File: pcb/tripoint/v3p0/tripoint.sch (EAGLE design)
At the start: 40 parts, among them T1 HHM1595A1, U1 STM32F091CC, U2 DW1000, U3 SKY13317, U4 LXDC2HN18A, X1 FA-128

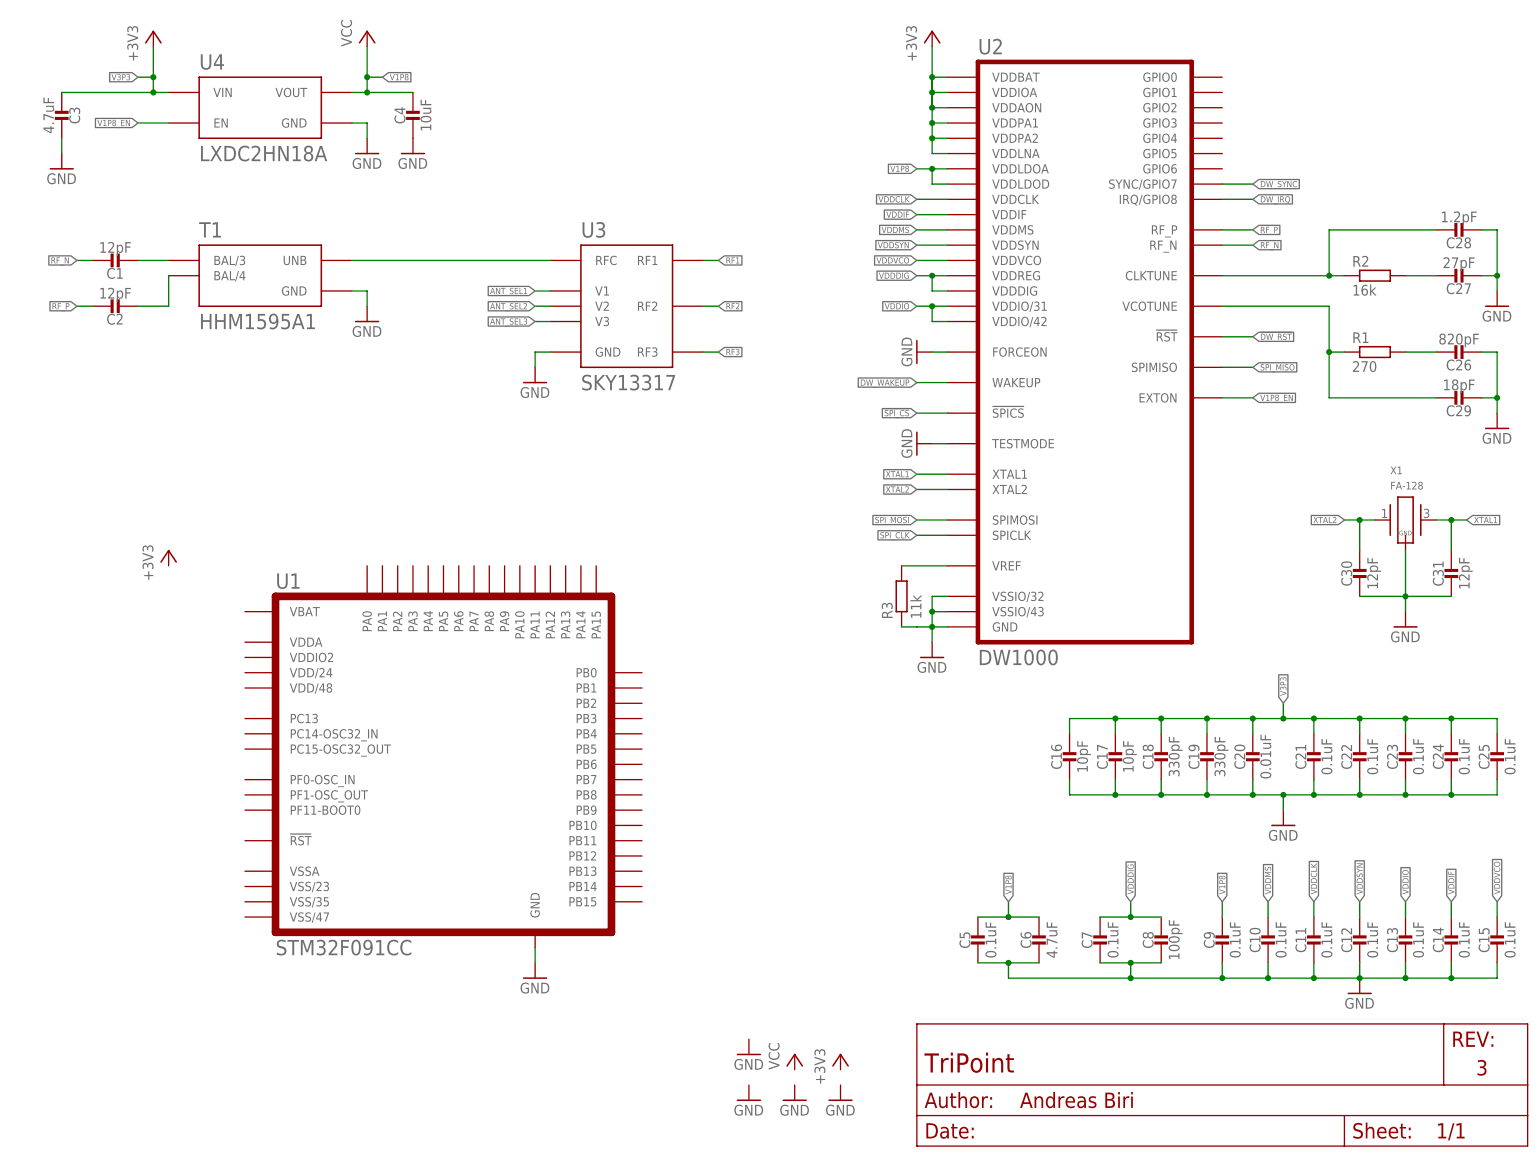
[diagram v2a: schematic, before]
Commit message: added oscillators
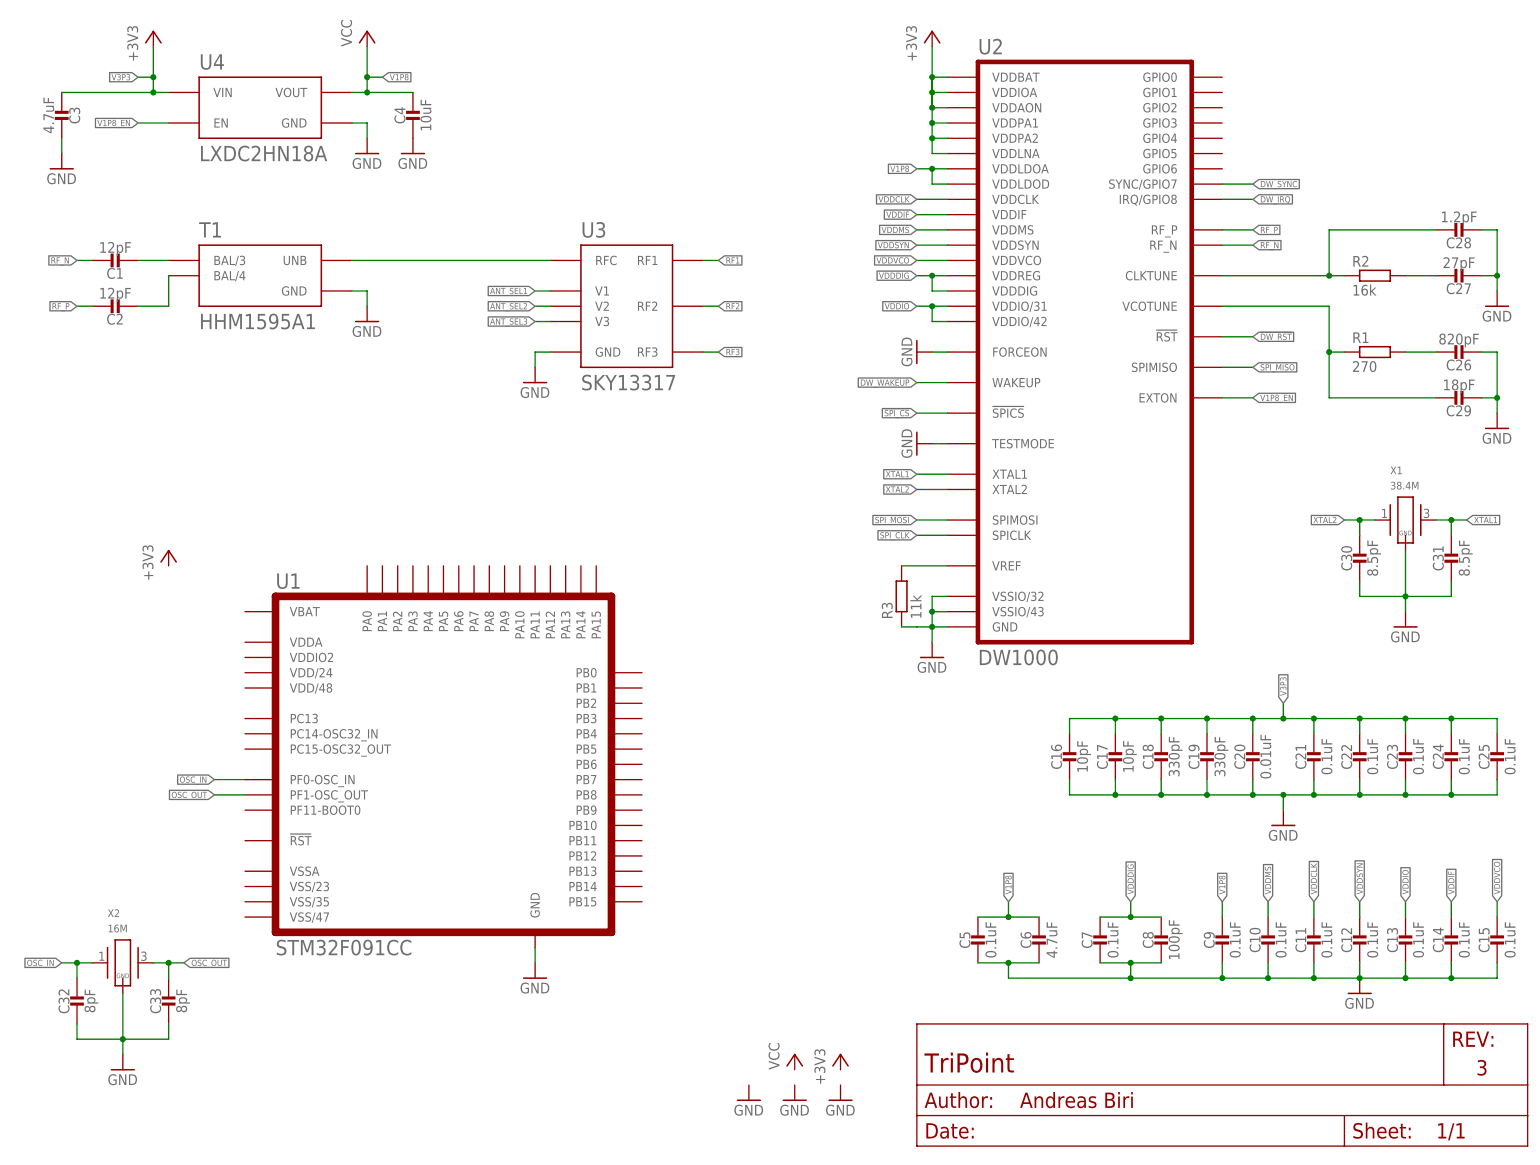
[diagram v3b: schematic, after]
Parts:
- added C32, C33: 8pF, passives:CAPACITOR0201_CAP
- added X2: 16M, crystals:FA-20H
- C30, C31: value 12pF -> 8.5pF
- X1: value FA-128 -> 38.4M; device crystals:FA-128 -> crystals:FA-20H; DESCRIPTION (none) -> 38.4MHz ±10ppm Crystal 8.5pF 40 Ohms 4-SMD, No Lead; DIGIKEY (none) -> SER3631CT-ND
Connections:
- new net OSC_IN: C32.1, U1.PF0-OSC_IN, X2.1
- new net OSC_OUT: C33.1, U1.PF1-OSC_OUT, X2.2
- net GND: now also C32.2, C33.2, X2.GND
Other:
- moved on the sheet: C30, C31
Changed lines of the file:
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@@
 <part name="SUPPLY17" library="umich" deviceset="GND" device=""/>
 <part name="SUPPLY18" library="umich" deviceset="GND" device=""/>
-<part name="X1" library="crystals" deviceset="FA-128" device=""/>
-<part name="C30" library="passives" deviceset="CAPACITOR" device="0201_CAP" value="12pF"/>
-<part name="C31" library="passives" deviceset="CAPACITOR" device="0201_CAP" value="12pF"/>
+<part name="C30" library="passives" deviceset="CAPACITOR" device="0201_CAP" value="8.5pF"/>
+<part name="C31" library="passives" deviceset="CAPACITOR" device="0201_CAP" value="8.5pF"/>
 <part name="+3V1" library="supply1" library_urn="urn:adsk.eagle:library:371" deviceset="+3V3" device=""/>
 <part name="+3V3" library="supply1" library_urn="urn:adsk.eagle:library:371" deviceset="+3V3" device=""/>
+<part name="C32" library="passives" deviceset="CAPACITOR" device="0201_CAP" value="8pF"/>
+<part name="C33" library="passives" deviceset="CAPACITOR" device="0201_CAP" value="8pF"/>
+<part name="X1" library="crystals" deviceset="FA-20H" device="" value="38.4M">
+<attribute name="DESCRIPTION" value="38.4MHz ±10ppm Crystal 8.5pF 40 Ohms 4-SMD, No Lead"/>
+<attribute name="DIGIKEY" value="SER3631CT-ND"/>
+</part>
+<part name="X2" library="crystals" deviceset="FA-20H" device="" value="16M">
+<attribute name="DESCRIPTION" value="16MHz ±10ppm Crystal 8pF 80 Ohms 4-SMD, No Lead"/>
+<attribute name="DIGIKEY" value="SER3913CT-ND"/>
+</part>
 </parts>
 <sheets>
@@
 <instance part="C29" gate="G$1" x="241.3" y="124.46" rot="R90"/>
 <instance part="SUPPLY12" gate="1" x="152.4" y="132.08" rot="R270"/>
-<instance part="SUPPLY13" gate="1" x="124.46" y="15.24"/>
+<instance part="SUPPLY13" gate="1" x="20.32" y="12.7"/>
 <instance part="SUPPLY14" gate="1" x="124.46" y="7.62"/>
 <instance part="SUPPLY15" gate="1" x="152.4" y="116.84" rot="R270"/>
@@
 <instance part="SUPPLY17" gate="1" x="154.94" y="81.28"/>
 <instance part="SUPPLY18" gate="1" x="233.68" y="86.36"/>
-<instance part="X1" gate="G$1" x="233.68" y="104.14"/>
-<instance part="C30" gate="G$1" x="226.06" y="96.52"/>
-<instance part="C31" gate="G$1" x="241.3" y="96.52"/>
+<instance part="C30" gate="G$1" x="226.06" y="99.06"/>
+<instance part="C31" gate="G$1" x="241.3" y="99.06"/>
 <instance part="+3V1" gate="G$1" x="27.94" y="99.06"/>
 <instance part="+3V3" gate="G$1" x="139.7" y="15.24"/>
+<instance part="C32" gate="G$1" x="12.7" y="25.4"/>
+<instance part="C33" gate="G$1" x="27.94" y="25.4"/>
+<instance part="X1" gate="X1" x="233.68" y="104.14">
+<attribute name="DIGIKEY" x="233.68" y="104.14" size="1.778" layer="96" display="off"/>
+<attribute name="DESCRIPTION" x="233.68" y="104.14" size="1.778" layer="96" display="off"/>
+</instance>
+<instance part="X2" gate="X1" x="20.32" y="30.48">
+<attribute name="DIGIKEY" x="20.32" y="30.48" size="1.778" layer="96" display="off"/>
+<attribute name="DESCRIPTION" x="20.32" y="30.48" size="1.778" layer="96" display="off"/>
+</instance>
 </instances>
 <busses>
@@
 </segment>
 <segment>
+<pinref part="U2" gate="U1" pin="TESTMODE"/>
+<wire x1="157.48" y1="116.84" x2="154.94" y2="116.84" width="0.1524" layer="91"/>
+<pinref part="SUPPLY15" gate="1" pin="GND"/>
+</segment>
+<segment>
+<pinref part="U2" gate="U1" pin="FORCEON"/>
+<wire x1="157.48" y1="132.08" x2="154.94" y2="132.08" width="0.1524" layer="91"/>
+<pinref part="SUPPLY12" gate="1" pin="GND"/>
+</segment>
+<segment>
 <pinref part="C30" gate="G$1" pin="2"/>
+<wire x1="226.06" y1="93.98" x2="226.06" y2="91.44" width="0.1524" layer="91"/>
 <pinref part="C31" gate="G$1" pin="2"/>
 <wire x1="226.06" y1="91.44" x2="233.68" y2="91.44" width="0.1524" layer="91"/>
 <wire x1="233.68" y1="91.44" x2="241.3" y2="91.44" width="0.1524" layer="91"/>
+<wire x1="241.3" y1="91.44" x2="241.3" y2="93.98" width="0.1524" layer="91"/>
+<pinref part="X1" gate="X1" pin="GND"/>
+<wire x1="233.68" y1="99.06" x2="233.68" y2="91.44" width="0.1524" layer="91"/>
+<junction x="233.68" y="91.44"/>
+<pinref part="SUPPLY18" gate="1" pin="GND"/>
 <wire x1="233.68" y1="91.44" x2="233.68" y2="88.9" width="0.1524" layer="91"/>
-<junction x="233.68" y="91.44"/>
-<pinref part="X1" gate="G$1" pin="GND"/>
-<wire x1="233.68" y1="99.06" x2="233.68" y2="91.44" width="0.1524" layer="91"/>
-<pinref part="SUPPLY18" gate="1" pin="GND"/>
-</segment>
-<segment>
-<pinref part="U2" gate="U1" pin="TESTMODE"/>
-<wire x1="157.48" y1="116.84" x2="154.94" y2="116.84" width="0.1524" layer="91"/>
-<pinref part="SUPPLY15" gate="1" pin="GND"/>
-</segment>
-<segment>
-<pinref part="U2" gate="U1" pin="FORCEON"/>
-<wire x1="157.48" y1="132.08" x2="154.94" y2="132.08" width="0.1524" layer="91"/>
-<pinref part="SUPPLY12" gate="1" pin="GND"/>
+</segment>
+<segment>
+<pinref part="C32" gate="G$1" pin="2"/>
+<wire x1="12.7" y1="20.32" x2="12.7" y2="17.78" width="0.1524" layer="91"/>
+<pinref part="C33" gate="G$1" pin="2"/>
+<wire x1="12.7" y1="17.78" x2="20.32" y2="17.78" width="0.1524" layer="91"/>
+<wire x1="20.32" y1="17.78" x2="27.94" y2="17.78" width="0.1524" layer="91"/>
+<wire x1="27.94" y1="17.78" x2="27.94" y2="20.32" width="0.1524" layer="91"/>
+<pinref part="X2" gate="X1" pin="GND"/>
+<wire x1="20.32" y1="25.4" x2="20.32" y2="17.78" width="0.1524" layer="91"/>
+<junction x="20.32" y="17.78"/>
+<pinref part="SUPPLY13" gate="1" pin="GND"/>
+<wire x1="20.32" y1="17.78" x2="20.32" y2="15.24" width="0.1524" layer="91"/>
 </segment>
 </net>
@@
 <net name="XTAL2" class="0">
 <segment>
-<pinref part="X1" gate="G$1" pin="1"/>
 <wire x1="228.6" y1="104.14" x2="226.06" y2="104.14" width="0.1524" layer="91"/>
 <pinref part="C30" gate="G$1" pin="1"/>
 <wire x1="226.06" y1="104.14" x2="223.52" y2="104.14" width="0.1524" layer="91"/>
-<wire x1="226.06" y1="104.14" x2="226.06" y2="99.06" width="0.1524" layer="91"/>
+<wire x1="226.06" y1="104.14" x2="226.06" y2="101.6" width="0.1524" layer="91"/>
 <junction x="226.06" y="104.14"/>
 <label x="223.52" y="104.14" size="1.016" layer="95" rot="R180" xref="yes"/>
+<pinref part="X1" gate="X1" pin="1"/>
 </segment>
 <segment>
@@
 <net name="XTAL1" class="0">
 <segment>
-<pinref part="X1" gate="G$1" pin="2"/>
-<wire x1="238.76" y1="104.14" x2="241.3" y2="104.14" width="0.1524" layer="91"/>
 <pinref part="C31" gate="G$1" pin="1"/>
 <wire x1="241.3" y1="104.14" x2="243.84" y2="104.14" width="0.1524" layer="91"/>
-<wire x1="241.3" y1="104.14" x2="241.3" y2="99.06" width="0.1524" layer="91"/>
+<wire x1="241.3" y1="104.14" x2="241.3" y2="101.6" width="0.1524" layer="91"/>
 <junction x="241.3" y="104.14"/>
 <label x="243.84" y="104.14" size="1.016" layer="95" xref="yes"/>
+<wire x1="241.3" y1="104.14" x2="238.76" y2="104.14" width="0.1524" layer="91"/>
+<pinref part="X1" gate="X1" pin="2"/>
 </segment>
 <segment>
@@
 </segment>
 </net>
+<net name="OSC_IN" class="0">
+<segment>
+<pinref part="C32" gate="G$1" pin="1"/>
+<wire x1="15.24" y1="30.48" x2="12.7" y2="30.48" width="0.1524" layer="91"/>
+<wire x1="12.7" y1="30.48" x2="12.7" y2="27.94" width="0.1524" layer="91"/>
+<wire x1="12.7" y1="30.48" x2="10.16" y2="30.48" width="0.1524" layer="91"/>
+<junction x="12.7" y="30.48"/>
+<label x="10.16" y="30.48" size="1.016" layer="95" rot="R180" xref="yes"/>
+<pinref part="X2" gate="X1" pin="1"/>
+</segment>
+<segment>
+<pinref part="U1" gate="U1" pin="PF0-OSC_IN"/>
+<wire x1="40.64" y1="60.96" x2="35.56" y2="60.96" width="0.1524" layer="91"/>
+<label x="35.56" y="60.96" size="1.016" layer="95" rot="R180" xref="yes"/>
+</segment>
+</net>
+<net name="OSC_OUT" class="0">
+<segment>
+<wire x1="25.4" y1="30.48" x2="27.94" y2="30.48" width="0.1524" layer="91"/>
+<pinref part="C33" gate="G$1" pin="1"/>
+<wire x1="27.94" y1="30.48" x2="27.94" y2="27.94" width="0.1524" layer="91"/>
+<wire x1="27.94" y1="30.48" x2="30.48" y2="30.48" width="0.1524" layer="91"/>
+<junction x="27.94" y="30.48"/>
+<label x="30.48" y="30.48" size="1.016" layer="95" xref="yes"/>
+<pinref part="X2" gate="X1" pin="2"/>
+</segment>
+<segment>
+<pinref part="U1" gate="U1" pin="PF1-OSC_OUT"/>
+<wire x1="40.64" y1="58.42" x2="35.56" y2="58.42" width="0.1524" layer="91"/>
+<label x="35.56" y="58.42" size="1.016" layer="95" rot="R180" xref="yes"/>
+</segment>
+</net>

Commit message: finished first draft of schematic
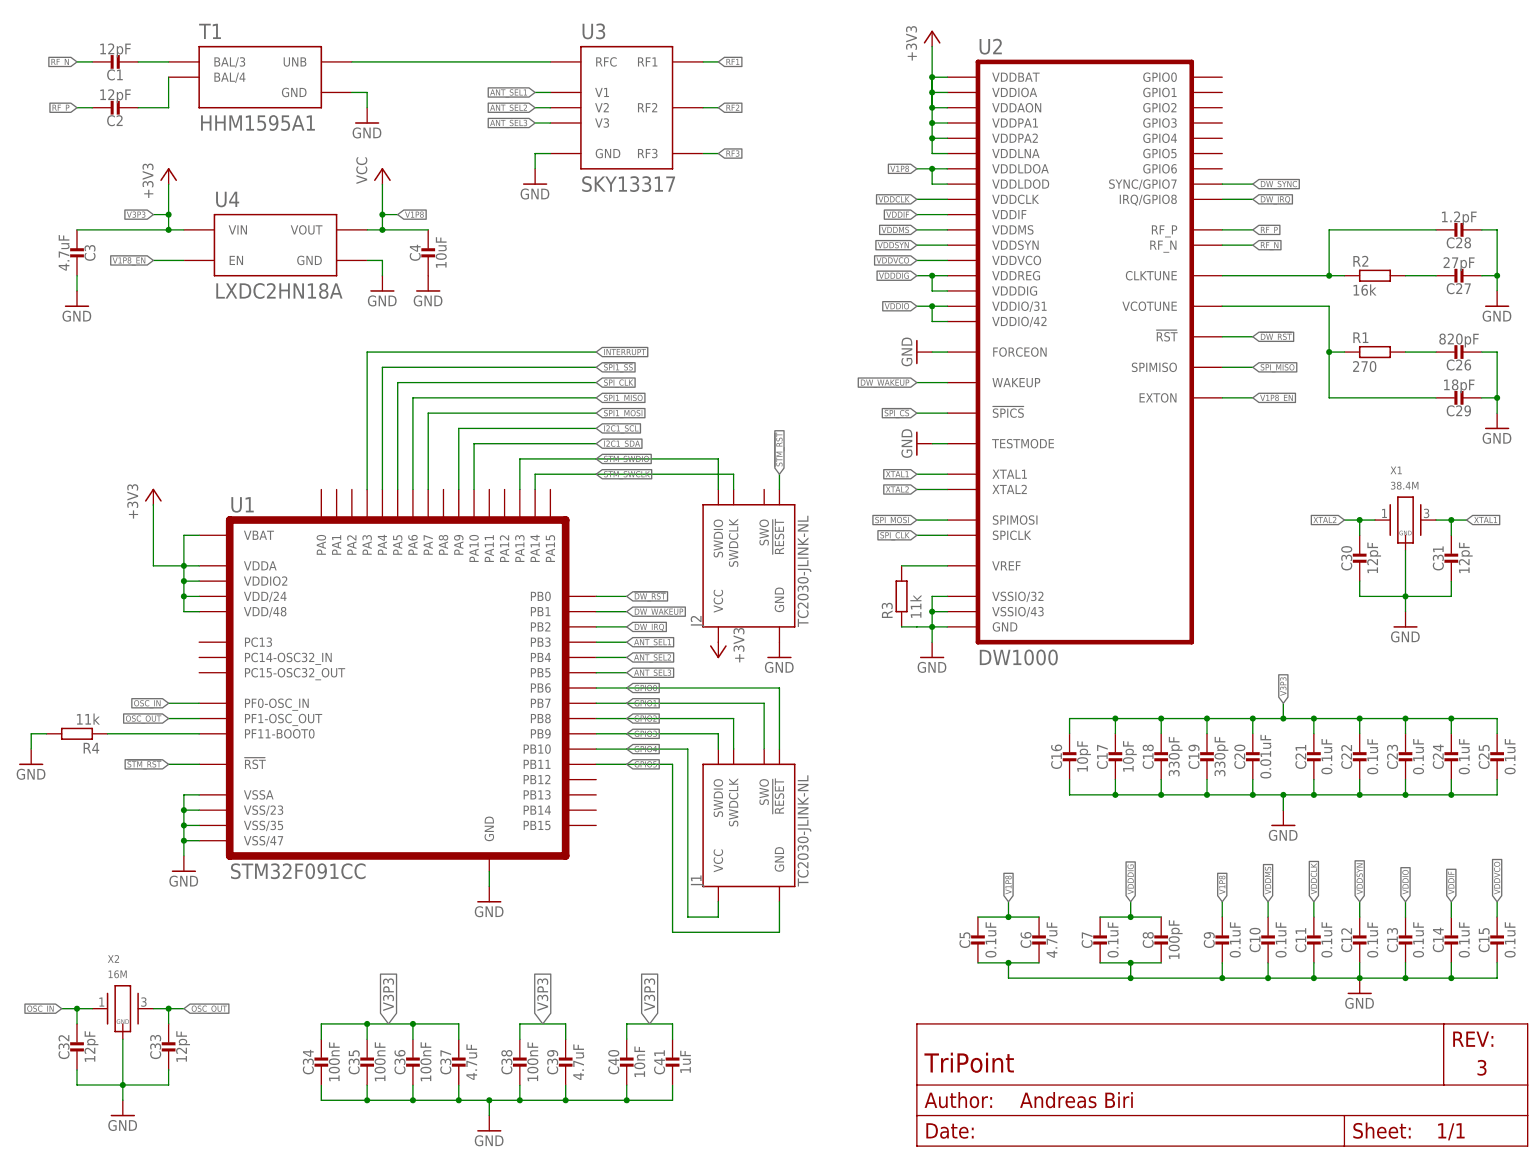
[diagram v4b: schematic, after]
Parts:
- added C34, C35, C36, C38: 100nF, passives:CAPACITOR0201_CAP
- added C37, C39: 4.7uF, passives:CAPACITOR0201_CAP
- added C40: 10nF, passives:CAPACITOR0201_CAP
- added C41: 1uF, passives:CAPACITOR0201_CAP
- added J1, J2: TC2030-JLINK-NL, connector:TC2030-JLINK-NL
- added R4: 11k, rcl:R-EU_R0201
- C30, C31: value 8.5pF -> 12pF
- C32, C33: value 8pF -> 12pF
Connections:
- new net !SPI1_SS: U1.PA4
- new net !STM_RST: J2.!RESET, U1.!RST
- new net +3V3: J2.VCC, U1.VBAT, U1.VDD/24, U1.VDD/48, U1.VDDA, U1.VDDIO2
- new net GPIO0: J1.!RESET, U1.PB6
- new net GPIO1: J1.SWO, U1.PB7
- new net GPIO2: J1.SWDCLK, U1.PB8
- new net GPIO3: J1.SWDIO, U1.PB9
- new net GPIO4: J1.VCC, U1.PB10
- new net GPIO5: J1.GND, U1.PB11
- new net I2C1_SCL: U1.PA9
- new net I2C1_SDA: U1.PA10
- new net INTERRUPT: U1.PA3
- new net N$8: R4.1, U1.PF11-BOOT0
- new net SPI1_MISO: U1.PA6
- new net SPI1_MOSI: U1.PA7
- new net STM_SWCLK: J2.SWDCLK, U1.PA14
- new net STM_SWDIO: J2.SWDIO, U1.PA13
- net !DW_RST: now also U1.PB0
- net ANT_SEL1: now also U1.PB3
- net ANT_SEL2: now also U1.PB4
- net ANT_SEL3: now also U1.PB5
- net DW_IRQ: now also U1.PB2
- net DW_WAKEUP: now also U1.PB1
- net GND: now also C34.2, C35.2, C36.2, C37.2, C38.2, C39.2, C40.2, C41.2, J2.GND, R4.2, U1.VSS/23, U1.VSS/35, U1.VSS/47, U1.VSSA
- net SPI_CLK: now also U1.PA5
- net V3P3: now also C34.1, C35.1, C36.1, C37.1, C38.1, C39.1, C40.1, C41.1
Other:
- note added: "BOOT0: Main Flash"
- note added: "DW1000"
- note added: "RF + DCDC"
- note added: "STM32F091CC"
- note added: "VBAT: No backup"
- note added: "VDD"
- note added: "VDDA"
- note added: "VDDIO2"
- moved on the sheet: C1, C2, C3, C32, C33, C4, T1, U1, U3, U4, X2
